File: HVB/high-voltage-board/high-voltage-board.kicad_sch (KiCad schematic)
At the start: 14 parts, among them J1 Conn_01x23, J11 HV-, J2 HECS, J3 HV+, J4 HV-, J5 HV+, J6 HV-, J7 Conn_01x02, J8 HV+, J9 Bender-LV

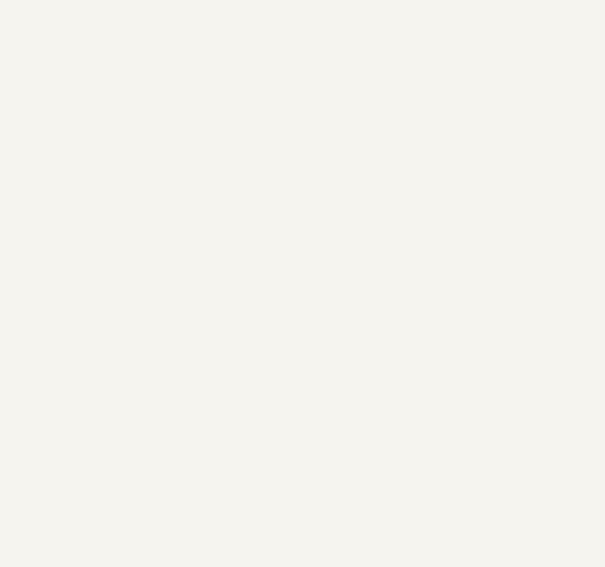
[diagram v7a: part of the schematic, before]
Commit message: adding mounting holes
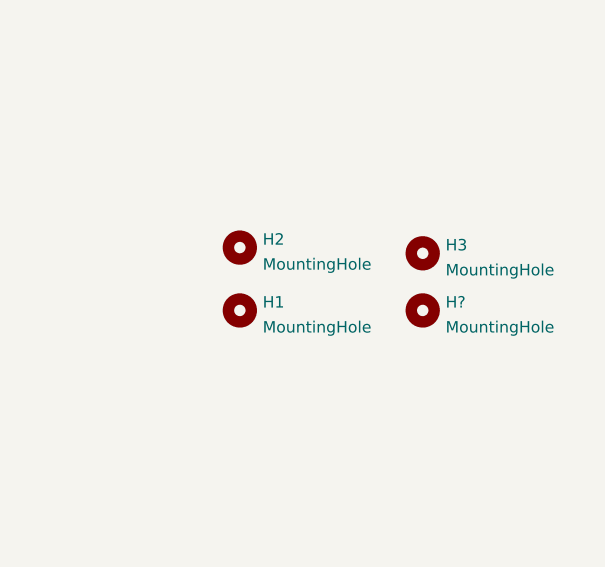
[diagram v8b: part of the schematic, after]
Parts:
- added H1, H2, H3, H?: MountingHole, MountingHole:MountingHole_3.2mm_M3, symbol Mechanical:MountingHole
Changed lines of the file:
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@@
     (pin "1")
+  )
+  (symbol (lib_id "Mechanical:MountingHole") (at 262.255 162.56 0) (unit 1)
+    (in_bom yes) (on_board yes) (fields_autoplaced)
+    (property "Reference" "H?" (id 0) (at 264.795 161.6515 0)
+      (effects (font (size 1.27 1.27)) (justify left))
+    )
+    (property "Value" "MountingHole" (id 1) (at 264.795 164.4266 0)
+      (effects (font (size 1.27 1.27)) (justify left))
+    )
+    (property "Footprint" "MountingHole:MountingHole_3.2mm_M3" (id 2) (at 262.255 162.56 0)
+      (effects (font (size 1.27 1.27)) hide)
+    )
+    (property "Datasheet" "~" (id 3) (at 262.255 162.56 0)
+      (effects (font (size 1.27 1.27)) hide)
+    )
   )
   (symbol (lib_id "power:+5VA") (at 29.21 161.29 270) (unit 1)
@@
     )
     (pin "1")
+  )
+  (symbol (lib_id "Mechanical:MountingHole") (at 241.935 155.575 0) (unit 1)
+    (in_bom yes) (on_board yes) (fields_autoplaced)
+    (property "Reference" "H2" (id 0) (at 244.475 154.6665 0)
+      (effects (font (size 1.27 1.27)) (justify left))
+    )
+    (property "Value" "MountingHole" (id 1) (at 244.475 157.4416 0)
+      (effects (font (size 1.27 1.27)) (justify left))
+    )
+    (property "Footprint" "MountingHole:MountingHole_3.2mm_M3" (id 2) (at 241.935 155.575 0)
+      (effects (font (size 1.27 1.27)) hide)
+    )
+    (property "Datasheet" "~" (id 3) (at 241.935 155.575 0)
+      (effects (font (size 1.27 1.27)) hide)
+    )
   )
   (symbol (lib_id "Device:R") (at 44.45 66.04 90) (unit 1)
@@
     (pin "1")
   )
+  (symbol (lib_id "Mechanical:MountingHole") (at 262.255 156.21 0) (unit 1)
+    (in_bom yes) (on_board yes) (fields_autoplaced)
+    (property "Reference" "H3" (id 0) (at 264.795 155.3015 0)
+      (effects (font (size 1.27 1.27)) (justify left))
+    )
+    (property "Value" "MountingHole" (id 1) (at 264.795 158.0766 0)
+      (effects (font (size 1.27 1.27)) (justify left))
+    )
+    (property "Footprint" "MountingHole:MountingHole_3.2mm_M3" (id 2) (at 262.255 156.21 0)
+      (effects (font (size 1.27 1.27)) hide)
+    )
+    (property "Datasheet" "~" (id 3) (at 262.255 156.21 0)
+      (effects (font (size 1.27 1.27)) hide)
+    )
+  )
   (symbol (lib_id "Device:R") (at 44.45 72.39 90) (unit 1)
     (in_bom yes) (on_board yes)
@@
     (pin "1")
     (pin "2")
+  )
+  (symbol (lib_id "Mechanical:MountingHole") (at 241.935 162.56 0) (unit 1)
+    (in_bom yes) (on_board yes) (fields_autoplaced)
+    (property "Reference" "H1" (id 0) (at 244.475 161.6515 0)
+      (effects (font (size 1.27 1.27)) (justify left))
+    )
+    (property "Value" "MountingHole" (id 1) (at 244.475 164.4266 0)
+      (effects (font (size 1.27 1.27)) (justify left))
+    )
+    (property "Footprint" "MountingHole:MountingHole_3.2mm_M3" (id 2) (at 241.935 162.56 0)
+      (effects (font (size 1.27 1.27)) hide)
+    )
+    (property "Datasheet" "~" (id 3) (at 241.935 162.56 0)
+      (effects (font (size 1.27 1.27)) hide)
+    )
   )
   (symbol (lib_id "power:+12V") (at 36.195 186.69 270) (mirror x) (unit 1)
@@
       (reference "F2") (unit 1) (value "2A") (footprint "Fuse:Fuseholder_Cylinder-5x20mm_Schurter_0031_8201_Horizontal_Open")
     )
+    (path "/af955edb-4849-4b65-b9d3-15c31dc09130"
+      (reference "H1") (unit 1) (value "MountingHole") (footprint "MountingHole:MountingHole_3.2mm_M3")
+    )
+    (path "/3c27dc86-1701-4cfb-9ebf-f044da440656"
+      (reference "H2") (unit 1) (value "MountingHole") (footprint "MountingHole:MountingHole_3.2mm_M3")
+    )
+    (path "/8c8730ef-8afc-440c-bb89-45bbd19f3ef4"
+      (reference "H3") (unit 1) (value "MountingHole") (footprint "MountingHole:MountingHole_3.2mm_M3")
+    )
+    (path "/245952d0-0e97-4e26-9005-0024054bd321"
+      (reference "H?") (unit 1) (value "MountingHole") (footprint "MountingHole:MountingHole_3.2mm_M3")
+    )
     (path "/00000000-0000-0000-0000-00005c830583"
